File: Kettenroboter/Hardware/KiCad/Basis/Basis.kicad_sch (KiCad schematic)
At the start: 106 parts, among them J1 691103110002, J10 691103110002, J11 Conn_01x03, J12 Conn_01x03, J13 Conn_01x03, J14 Conn_01x03, J15 Conn_01x01, J16 Conn_01x03, J17 Conn_01x03, J18 691103110002, J19 691103110002, J2 691103110002, J20 691103110002, J21 691103110002, J22 691103110002, J23 691103110002, J24 691103110002, J25 691103110002, J26 691103110002, J27 691103110002, J28 Conn_01x02, J3 691103110002, J4 691103110002, J5 691103110002, J6 691103110002, J7 691103110002, J8 691103110002, J9 691103110002, Q1 BSS138, Q2 BSS138, Q3 BSS138, Q4 BSS138, Q5 NMOS, Q6 NMOS, U2 NCP1117LPST33T3G, U3 SN74LS07

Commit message: final final final
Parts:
- removed D8: 1N5817, Diode_THT:D_DO-41_SOD81_P10.16mm_Horizontal, symbol Diode:1N5817
- added C17, C18, C19, C20: 10n, Capacitor_SMD:C_1206_3216Metric_Pad1.33x1.80mm_HandSolder, symbol Device:C
- added D11: 1N5817, Diode_THT:D_DO-41_SOD81_P10.16mm_Horizontal, symbol Diode:1N5817
- added D8: BAT46, Diode_THT:D_DO-35_SOD27_P7.62mm_Horizontal, symbol Diode:BAT46
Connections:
- net I2C0 -SDA - HV is gone; now on net I2C0 - SDA - HV: Q1.3 (D), R2.2
- net PWR-GND is gone; now on net GND: J25.1, Q5.3 (S), Q6.3 (S)
- net +12V: now also D11.2 (A); no longer J27.2
- net +3V3: now also C17.1, C18.1, C19.1, C20.1, D8.1 (K)
- net GND: now also J20.2, C17.2, C18.2, C19.2, C20.2; no longer H1.1, H2.1, H3.1, H4.1, H5.1, H6.1, J20.1
- net VBUS: no longer C1.1, U2.3 (INPUT)
- net VSYS: now also C1.1, U2.3 (INPUT)
- net V_D_out_ext: now also J20.1; no longer J20.2
- net at A1.36 (3V3): now also D8.2 (A)
- new net: D11.1 (K), J27.2
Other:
- moved on the sheet: C10, C7, C8, C9

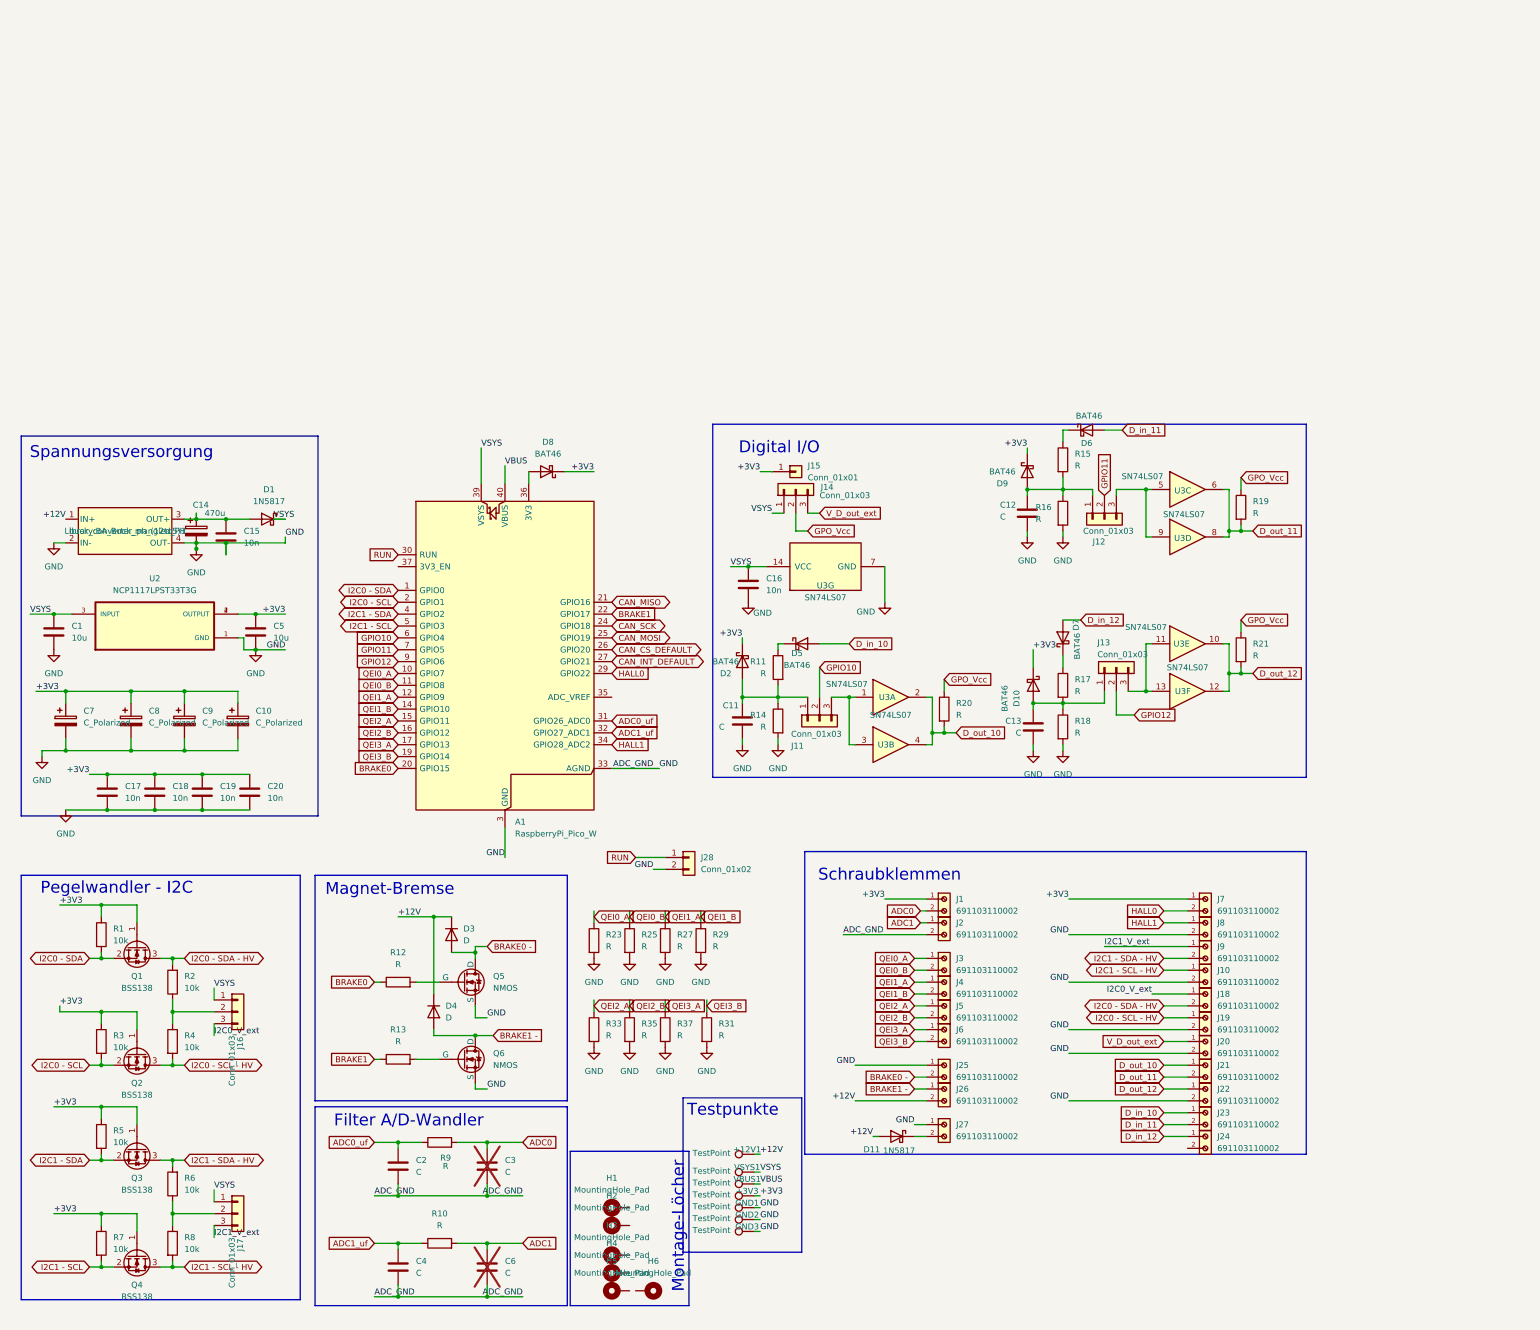
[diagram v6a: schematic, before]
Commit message: All Parts placed (BOM)
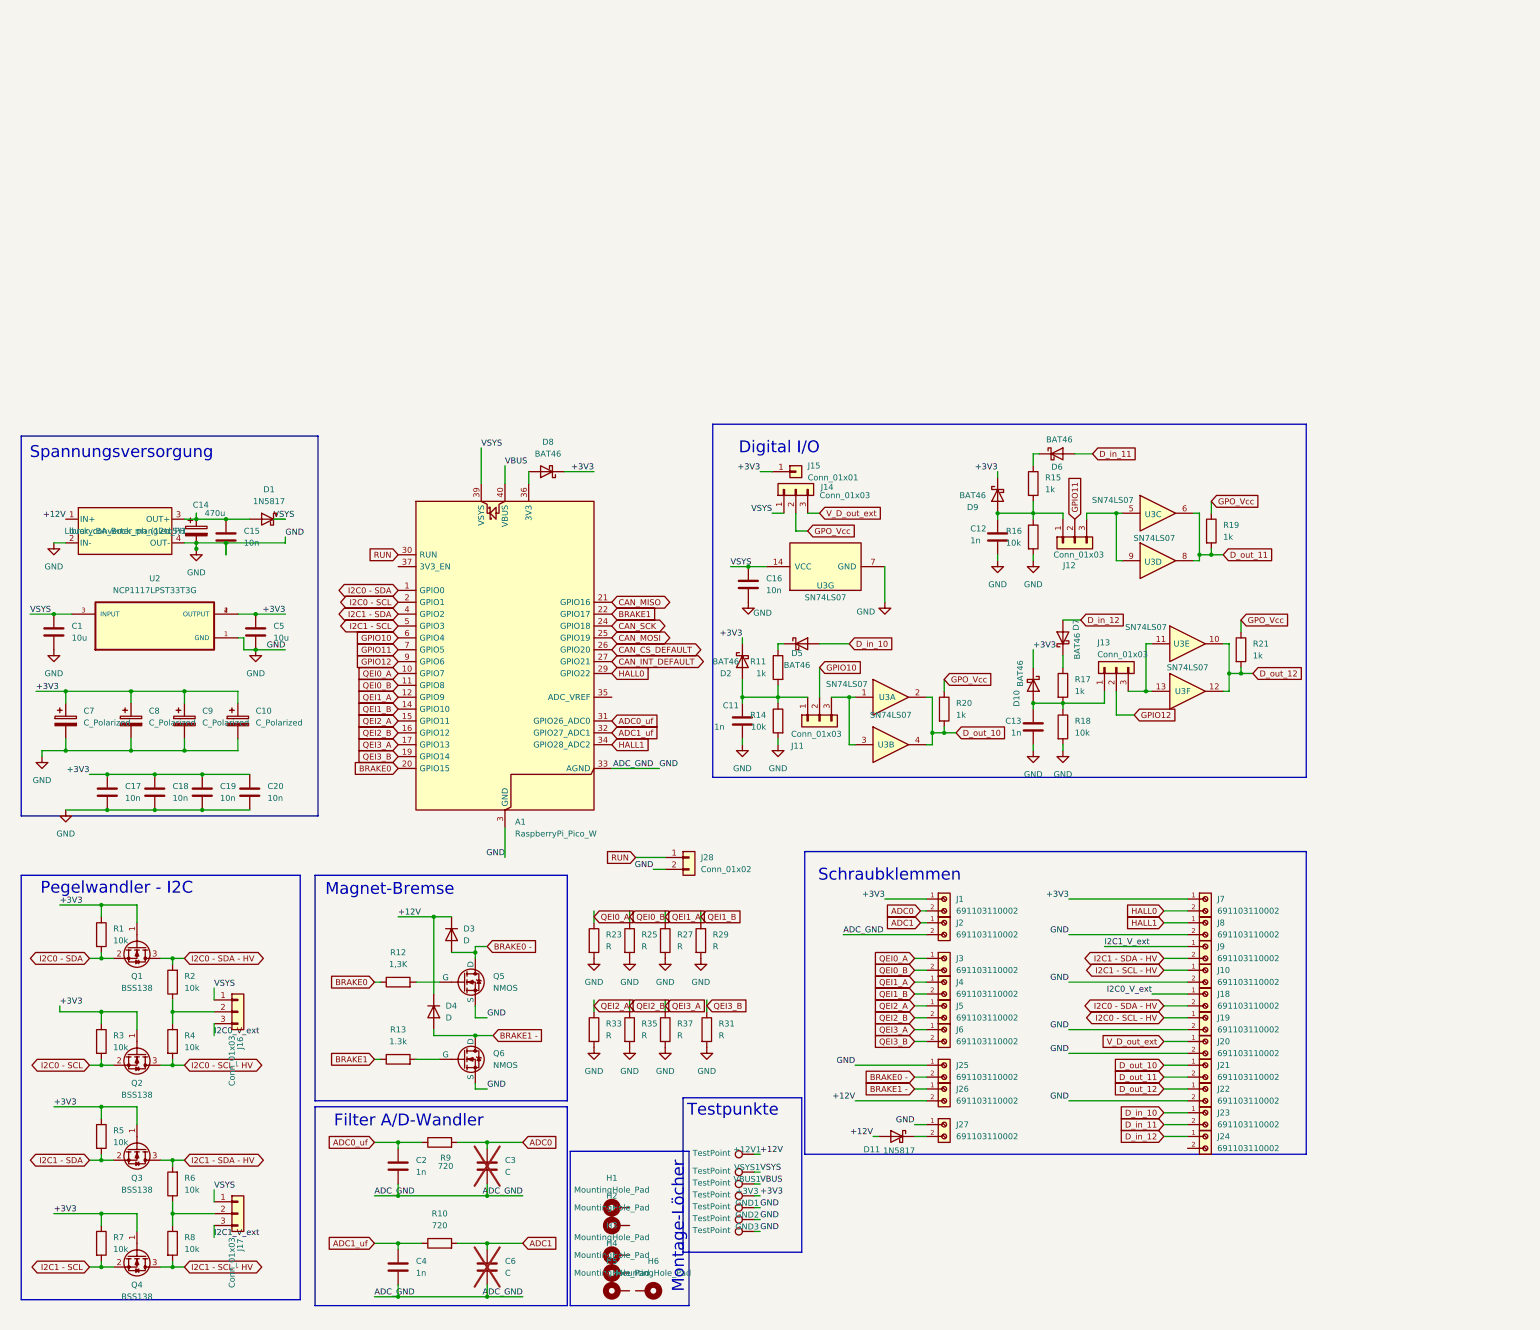
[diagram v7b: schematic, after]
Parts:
- C11, C12, C13, C2, C4: value C -> 1n
- R10, R9: value R -> 720
- R11, R15, R17, R19, R20, R21: value R -> 1k
- R12: value R -> 1,3K
- R13: value R -> 1.3k
- R14, R16, R18: value R -> 10k
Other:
- moved on the sheet: C12, D6, D9, J12, R15, R16, R19, U3C, U3D
